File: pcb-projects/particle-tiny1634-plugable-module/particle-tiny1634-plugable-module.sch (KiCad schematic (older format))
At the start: 32 parts, among them IC1 ATTINY1634-SU, P1 INTERFACE, P2 MCU_TEST

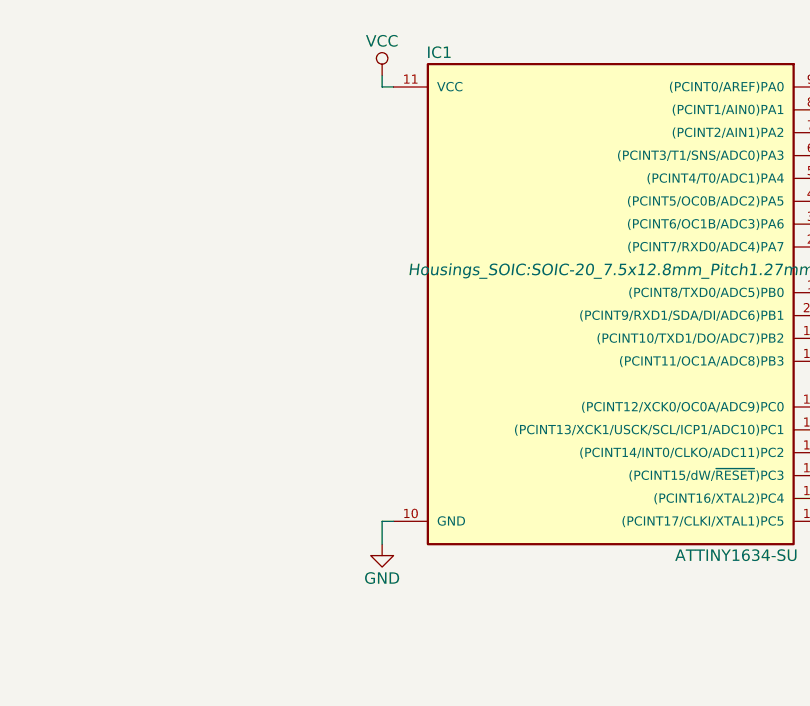
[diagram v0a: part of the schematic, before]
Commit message: added power supply capacitor
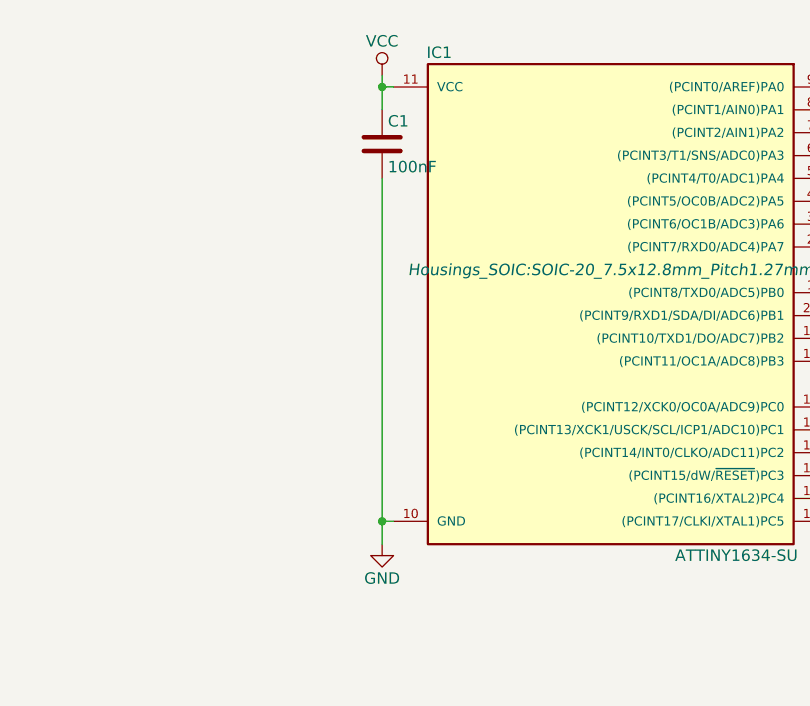
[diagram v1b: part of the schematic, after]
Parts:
- added C1: 100nF, Capacitors_SMD:C_1206_HandSoldering, symbol C
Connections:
- net GND: now also C1.2
- net VCC: now also C1.1
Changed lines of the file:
@@
 	850  3600 900  3600
 Wire Wire Line
-	850  3600 850  3700
+	850  2100 850  3700
 Wire Wire Line
 	900  1700 850  1700
 Wire Wire Line
-	850  1700 850  1650
+	850  1650 850  1800
 Wire Wire Line
 	1800 6300 1950 6300
@@
 Text Notes 850  5500 0    60   ~ 0
 Bridge
+$Comp
+L C C1
+U 1 1 56ADF2A8
+P 850 1950
+F 0 "C1" H 875 2050 50  0000 L CNN
+F 1 "100nF" H 875 1850 50  0000 L CNN
+F 2 "Capacitors_SMD:C_1206_HandSoldering" H 888 1800 50  0001 C CNN
+F 3 "" H 850 1950 50  0000 C CNN
+	1    850  1950
+	1    0    0    -1
+$EndComp
+Connection ~ 850  1700
+Connection ~ 850  3600
 $EndSCHEMATC
